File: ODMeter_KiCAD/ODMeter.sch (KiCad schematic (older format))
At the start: 9 parts, among them P1 Digital, P2 Analog, SW1 40-2390-00, U1 OPT101P, U2 NHD-0216XZ

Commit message: updated kicad
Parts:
- removed D1: TLCY5800, symbol Device:LED
- removed P1: Digital, Socket_Arduino_Micro:Socket_Strip_Arduino_1x17, symbol Connector_Generic:Conn_01x17
- removed P2: Analog, Socket_Arduino_Micro:Socket_Strip_Arduino_1x17, symbol Connector_Generic:Conn_01x17
- removed SW1: 40-2390-00, symbol Switch:SW_Push
- removed U1: OPT101P, digikey-footprints:DIP-8_W7.62mm, symbol ODMeter-rescue:OPT101P-AmbientOptical-ODMeter-rescue-ODMeter-rescue
- added D1: TLCY5800, symbol ODMeter-cache:Device_LED
- added SW1: 40-2390-00, symbol ODMeter-cache:Switch_SW_Push
- added U1: ArduinoMicro, symbol arduino:ArduinoMicro
- added U3: OPT101P, digikey-footprints:DIP-8_W7.62mm, symbol ODMeter-rescue:OPT101P-AmbientOptical-ODMeter-rescue-ODMeter-rescue
- R1: value 100R -> 100; footprint Resistor_THT:R_Axial_DIN0207_L6.3mm_D2.5mm_P10.16mm_Horizontal -> (none)
- R2: value 100k -> 1.8M; footprint Resistor_THT:R_Axial_DIN0207_L6.3mm_D2.5mm_P10.16mm_Horizontal -> (none)
- RV1: value 500k -> 100k
- U2: value NHD-0216XZ -> NHD-0216XZ-FSW-GBW
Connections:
- net +5V: now also U2.1 (VSS), U3.1 (VS); no longer U2.2 (VDD)
- net GND: now also U2.2 (VDD), SW1.1, U1.~ (VIN), U3.3 (V-), U3.8 (COM); no longer RV1.3, U2.1 (VSS)
- net at R2.2: now also RV1.1
- net at R2.1: now also U3.2 (-IN); no longer RV1.1
- net at R1.1: now also D1.1 (K)
- net 10(A10): no longer names the net of U2.12 (DB5)
- net 10(A10): now also U1.~ (VIN)
- net 11(**): no longer names the net of U2.13 (DB6)
- net 11(**): now also U1.~ (VIN)
- net 12(A11): no longer names the net of U2.14 (DB7)
- net 12(A11): now also U1.~ (VIN)
- net 5(**): no longer names the net of U2.3 (VO)
- net 5(**): now also U1.~ (VIN)
- net 6(**/A7): no longer names the net of U2.4 (RS)
- net 6(**/A7): now also U1.~ (VIN)
- net 7: no longer names the net of U2.5 (R/W)
- net 7: now also U1.~ (VIN)
- net 8(A8): no longer names the net of U2.6 (E)
- net 8(A8): now also U1.~ (VIN)
- net 9(**/A9): no longer names the net of U2.11 (DB4)
- net 9(**/A9): now also U1.~ (VIN)
- net A0: no longer names the net of RV1.2
- net A0: now also U1.~ (VIN), U3.5 (OUT)
- new net: SW1.2, U1.~ (VIN)
- new net: D1.2 (A), U1.~ (VIN)
- no-connect marks 7 -> 25
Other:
- note added: "16x2 Character LCD\n"
- note added: "590nm LED\n"
- note added: "Arduino Micro\n"
- note added: "Photodiode\n"
- note removed: "1"
- note removed: "16x2 Character LCD"
- note removed: "650nm LED"
- note removed: "Arduino Micro"
- note removed: "Photodiode"

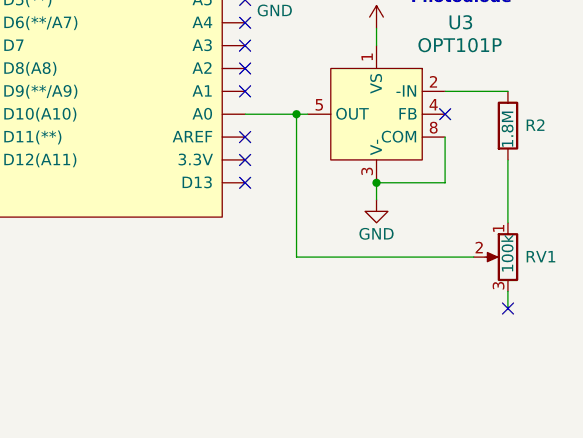
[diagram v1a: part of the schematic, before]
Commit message: Connected wiper to 3rd pin
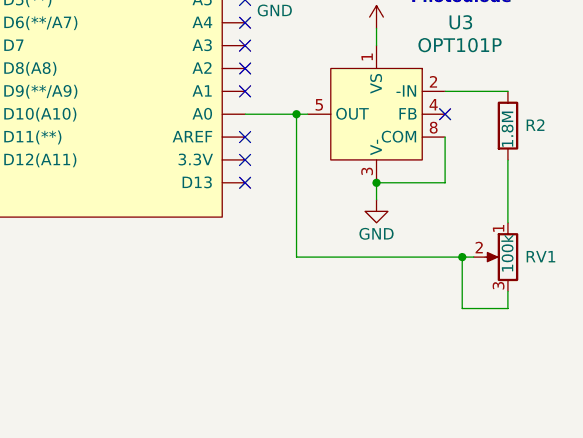
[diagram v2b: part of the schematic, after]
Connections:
- net at RV1.2, U1.~ (VIN), U3.5 (OUT): now also RV1.3
- no-connect marks 25 -> 24
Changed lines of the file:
@@
 	6650 4125 6650 4750
 Wire Wire Line
-	6650 4750 7425 4750
+	6650 4750 7375 4750
 Wire Wire Line
 	7575 4325 7575 4600
@@
 Wire Wire Line
 	7575 4900 7575 4975
-NoConn ~ 7575 4975
+Wire Wire Line
+	7575 4975 7375 4975
+Wire Wire Line
+	7375 4975 7375 4750
+Connection ~ 7375 4750
+Wire Wire Line
+	7375 4750 7425 4750
 $EndSCHEMATC

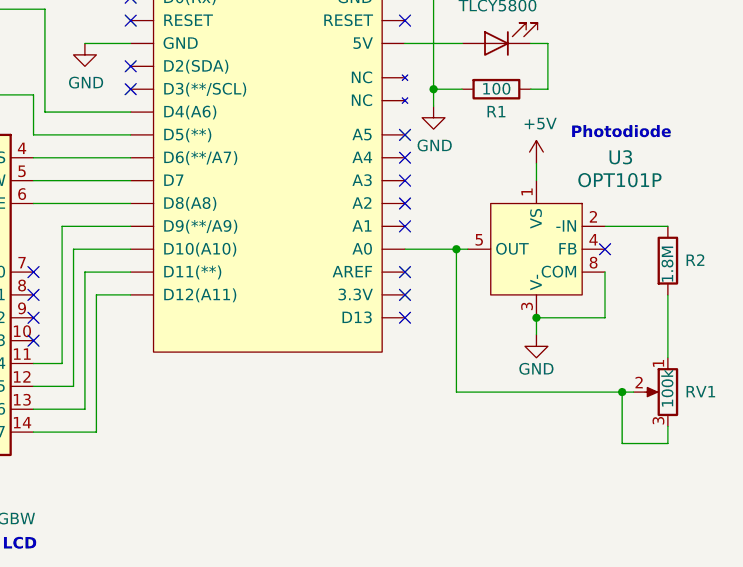
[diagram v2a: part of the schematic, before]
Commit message: Fixed AREF on schematic
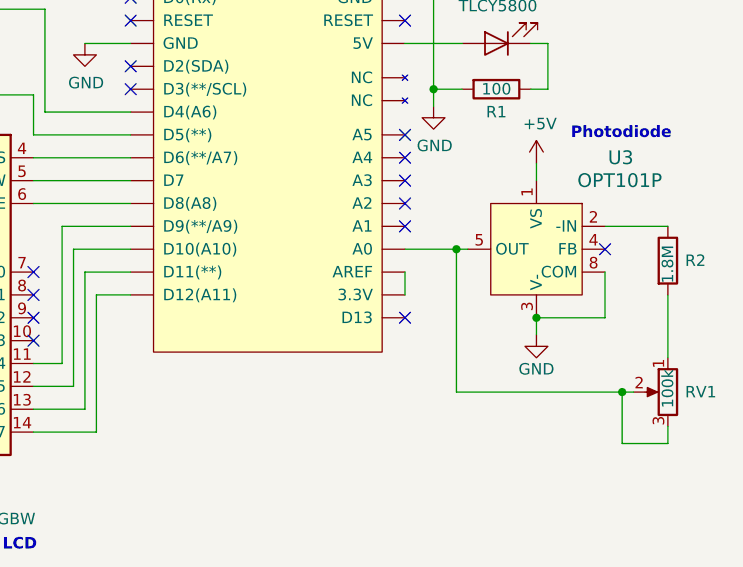
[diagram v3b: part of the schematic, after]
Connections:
- no-connect marks 24 -> 22
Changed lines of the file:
@@
 Wire Wire Line
 	7575 4325 7575 4600
-NoConn ~ 6425 4225
-NoConn ~ 6425 4325
 NoConn ~ 6425 4425
 Wire Wire Line
@@
 Wire Wire Line
 	7375 4750 7425 4750
+Wire Wire Line
+	6425 4225 6425 4325
 $EndSCHEMATC
